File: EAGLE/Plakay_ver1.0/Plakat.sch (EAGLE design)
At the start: 26 parts

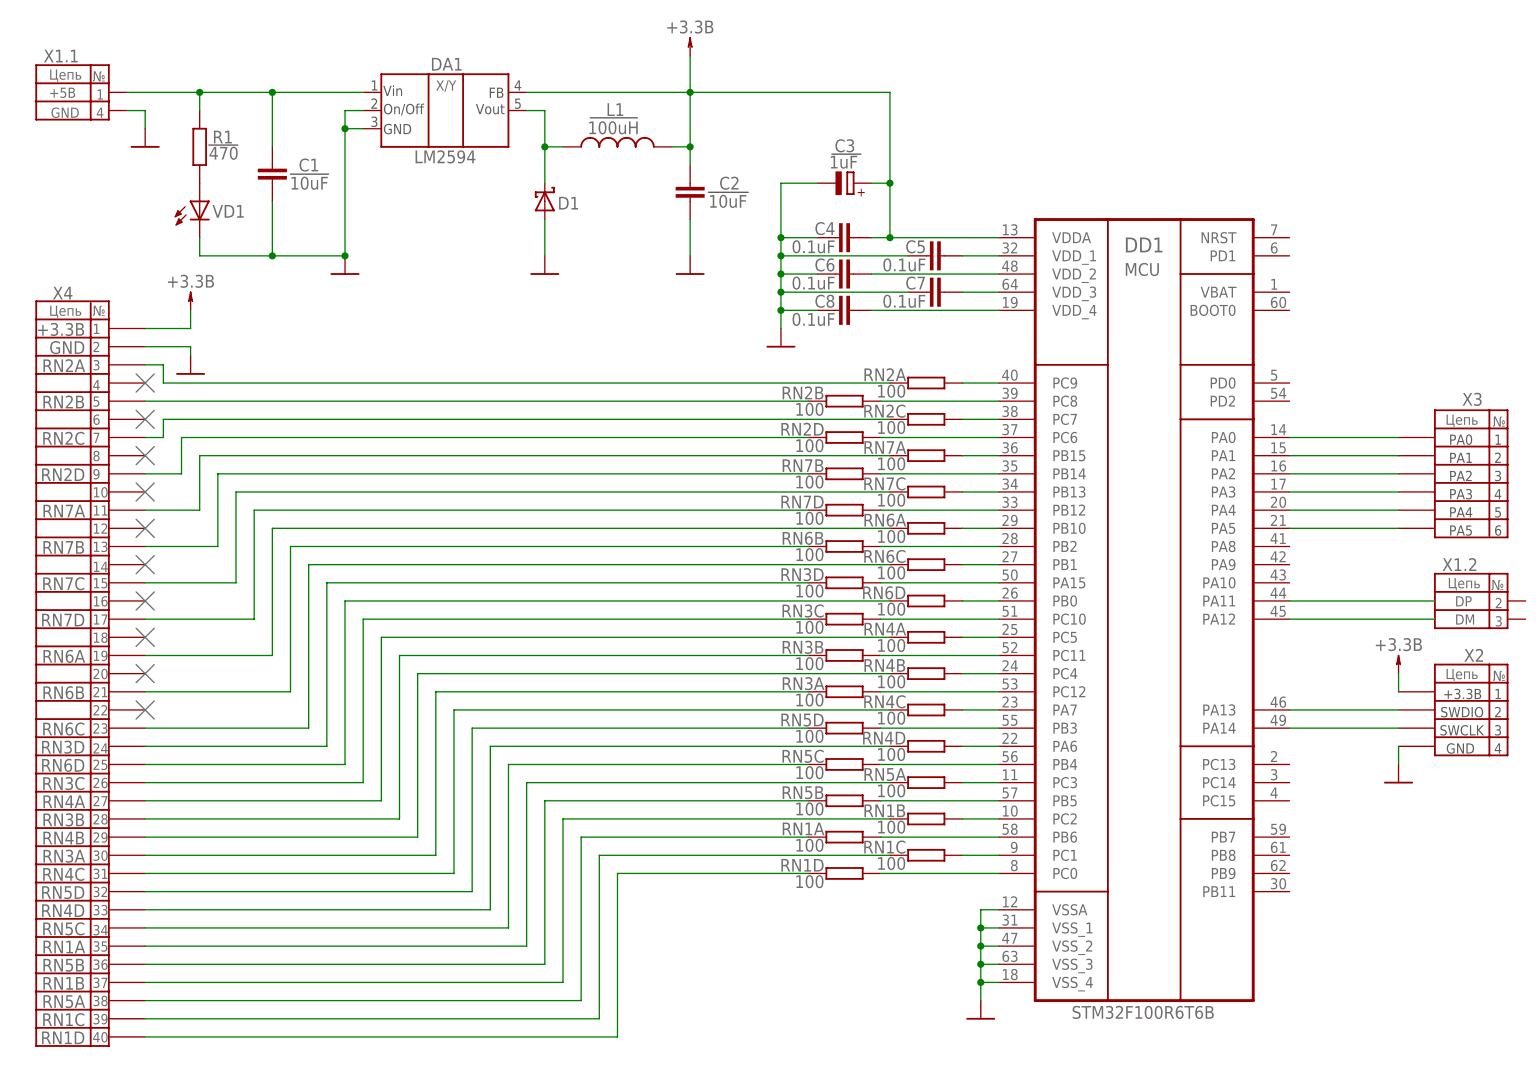
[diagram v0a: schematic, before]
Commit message: Created Plakat_ver2.0
This version of PCB is up-to-date. Change list:
	1. Added RESET button
	2. Deleted resistor-arrays
	3. Modified SWD communication
	4. VBAT pull-up to VCC
	5. BOOT0 pulled-down throught resistor
	6. Added VD2 and VD3
	7. Fixed schematic - now capacitors doted to VCC
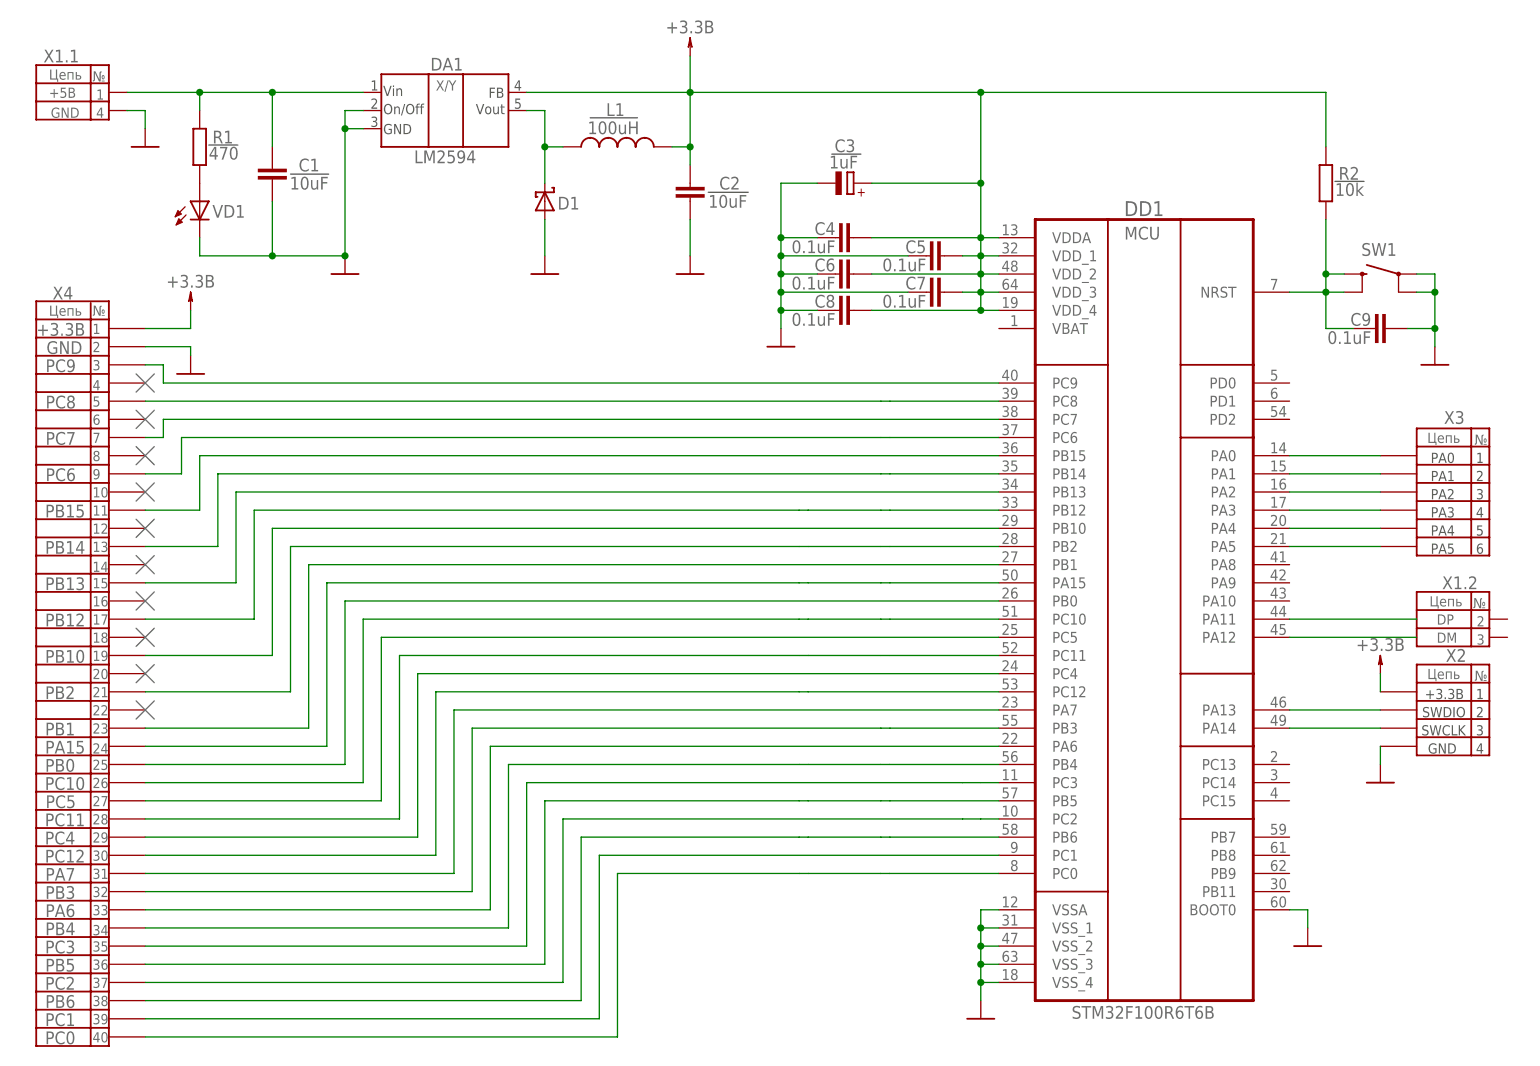
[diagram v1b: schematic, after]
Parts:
- removed RN1, RN2, RN3, RN4, RN5, RN6, RN7: 100, resistor-dil:4R-N0603-ARC
- added C9: 0.1uF, rcl:C-EUC0805
- added R2: 10k, eagle-ltspice:R
- added SW1: DTSM-6, switch-tact:DTSM-6
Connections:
- removed net N$12: DD1.PC7, RN2C.1
- removed net N$13: DD1.PC6, RN2D.1
- removed net N$14: DD1.PB15, RN7A.2
- removed net N$15: DD1.PB14, RN7B.2
- removed net N$16: DD1.PB13, RN7C.2
- removed net N$17: DD1.PB12, RN7D.2
- removed net N$18: DD1.PB10, RN6A.2
- removed net N$19: DD1.PB2, RN6B.2
- removed net N$20: DD1.PB1, RN6C.2
- removed net N$21: DD1.PA15, RN3D.2
- removed net N$22: DD1.PB0, RN6D.2
- removed net N$23: DD1.PC10, RN3C.1
- removed net N$24: DD1.PC5, RN4A.1
- removed net N$25: DD1.PC11, RN3B.1
- removed net N$26: DD1.PC4, RN4B.1
- removed net N$28: DD1.PA7, RN4C.2
- removed net N$29: DD1.PB3, RN5D.2
- removed net N$31: DD1.PA6, RN4D.2
- removed net N$32: DD1.PB4, RN5C.2
- removed net N$33: DD1.PC3, RN5A.2
- removed net N$34: DD1.PB5, RN5B.2
- removed net N$35: DD1.PC2, RN1B.1
- removed net N$36: DD1.PB6, RN1A.1
- removed net N$37: DD1.PC1, RN1C.1
- removed net N$38: DD1.PC0, RN1D.1
- removed net N$5: DD1.PC9, RN2A.1
- removed net N$56: RN3A.2, X4.30
- removed net N$68: C7.2, DD1.VDD_3
- removed net N$69: C6.2, DD1.VDD_2
- removed net N$7: DD1.PC8, RN2B.1
- removed net N$71: C8.2, DD1.VDD_4
- net GND: now also C9.2, DD1.BOOT0, DD1.VSSA, DD1.VSS_1, DD1.VSS_2, DD1.VSS_3, DD1.VSS_4, SW1.1, SW1.2
- net N$27: now also X4.30; no longer RN3A.1
- net N$30: now also C9.1, DD1.NRST, R2.1, SW1.3, SW1.4; no longer C5.2, DD1.VDD_1
- net N$39: now also DD1.PC9; no longer RN2A.2
- net N$40: now also DD1.PC8; no longer RN2B.2
- net N$41: now also DD1.PC7; no longer RN2C.2
- net N$42: now also DD1.PC6; no longer RN2D.2
- net N$43: now also DD1.PB15; no longer RN7A.1
- net N$44: now also DD1.PB14; no longer RN7B.1
- net N$45: now also DD1.PB13; no longer RN7C.1
- net N$46: now also DD1.PB12; no longer RN7D.1
- net N$47: now also DD1.PB10; no longer RN6A.1
- net N$48: now also DD1.PB2; no longer RN6B.1
- net N$49: now also DD1.PB1; no longer RN6C.1
- net N$50: now also DD1.PA15; no longer RN3D.1
- net N$51: now also DD1.PB0; no longer RN6D.1
- net N$52: now also DD1.PC10; no longer RN3C.2
- net N$53: now also DD1.PC5; no longer RN4A.2
- net N$54: now also DD1.PC11; no longer RN3B.2
- net N$55: now also DD1.PC4; no longer RN4B.2
- net N$57: now also DD1.PA7; no longer RN4C.1
- net N$58: now also DD1.PB3; no longer RN5D.1
- net N$59: now also DD1.PA6; no longer RN4D.1
- net N$60: now also DD1.PB4; no longer RN5C.1
- net N$61: now also DD1.PC3; no longer RN5A.1
- net N$62: now also DD1.PB5; no longer RN5B.1
- net N$63: now also DD1.PC2; no longer RN1B.2
- net N$64: now also DD1.PB6; no longer RN1A.2
- net N$65: now also DD1.PC1; no longer RN1C.2
- net N$66: now also DD1.PC0; no longer RN1D.2
- net VCC: now also C5.2, C6.2, C7.2, C8.2, DD1.VDD_1, DD1.VDD_2, DD1.VDD_3, DD1.VDD_4, R2.2
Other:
- note added: "PA15"
- note added: "PA6"
- note added: "PA7"
- note added: "PB0"
- note added: "PB1"
- note added: "PB10"
- note added: "PB12"
- note added: "PB13"
- note added: "PB14"
- note added: "PB15"
- note added: "PB2"
- note added: "PB3"
- note added: "PB4"
- note added: "PB5"
- note added: "PB6"
- note added: "PC0"
- note added: "PC1"
- note added: "PC10"
- note added: "PC11"
- note added: "PC12"
- note added: "PC2"
- note added: "PC3"
- note added: "PC4"
- note added: "PC5"
- note added: "PC6"
- note added: "PC7"
- note added: "PC8"
- note added: "PC9"
- note removed: "RN1A"
- note removed: "RN1B"
- note removed: "RN1C"
- note removed: "RN1D"
- note removed: "RN2A"
- note removed: "RN2B"
- note removed: "RN2C"
- note removed: "RN2D"
- note removed: "RN3A"
- note removed: "RN3B"
- note removed: "RN3C"
- note removed: "RN3D"
- note removed: "RN4A"
- note removed: "RN4B"
- note removed: "RN4C"
- note removed: "RN4D"
- note removed: "RN5A"
- note removed: "RN5B"
- note removed: "RN5C"
- note removed: "RN5D"
- note removed: "RN6A"
- note removed: "RN6B"
- note removed: "RN6C"
- note removed: "RN6D"
- note removed: "RN7A"
- note removed: "RN7B"
- note removed: "RN7C"
- note removed: "RN7D"
- moved on the sheet: X1.2, X2, X3
